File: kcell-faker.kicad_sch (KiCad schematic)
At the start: 19 parts, among them J4 DBG, SW1 BOOT, SW2 RST, SW3 UP, SW4 DOWN, U6 ESP32-S3-MINI-1

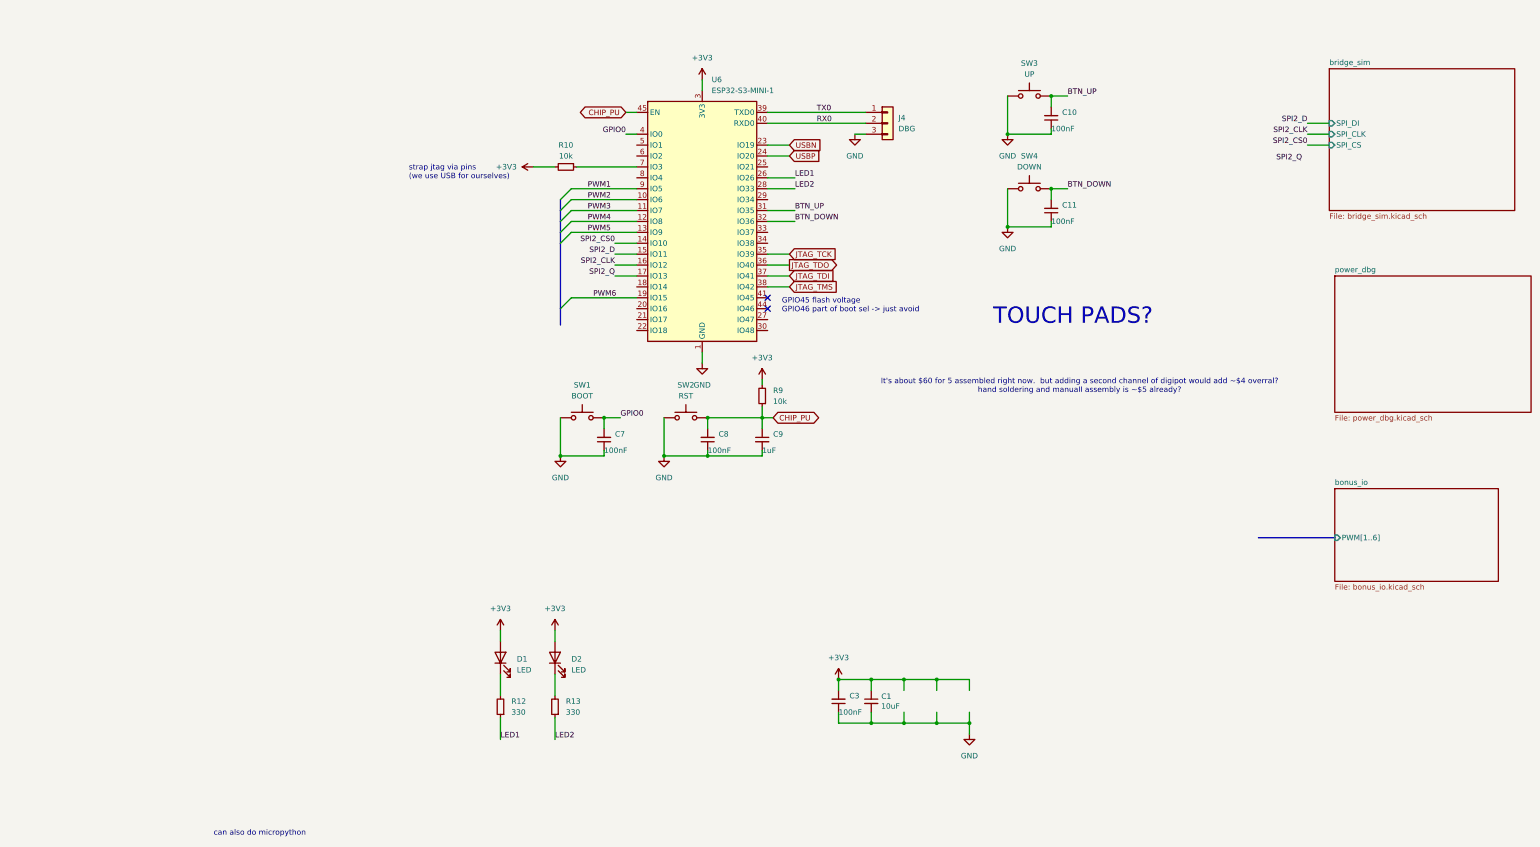
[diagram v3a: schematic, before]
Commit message: cleanup a bit
use red+green leds, sch on .100 grid, hook up more pins
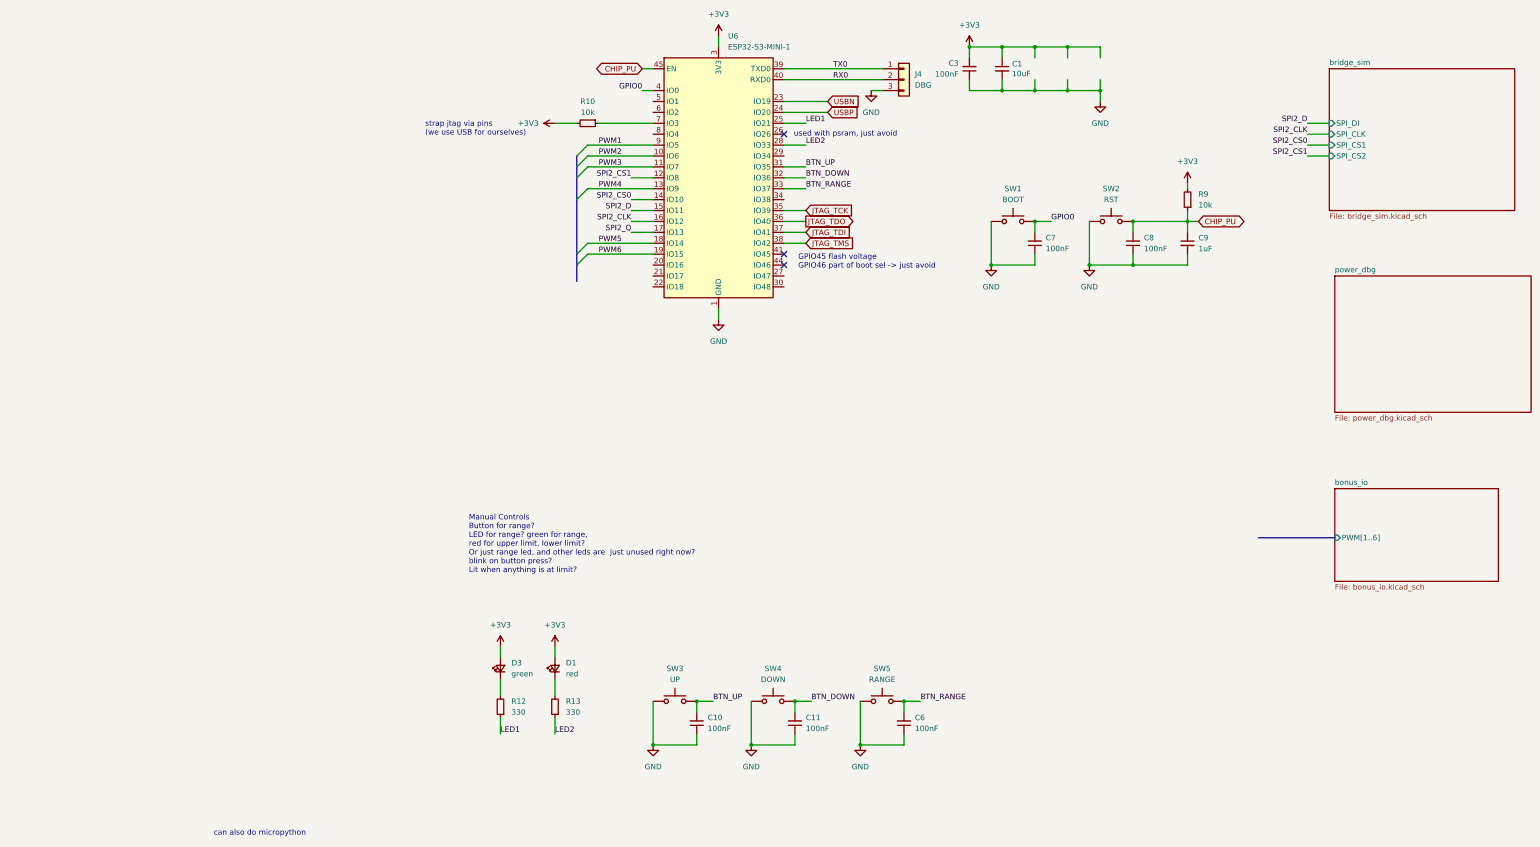
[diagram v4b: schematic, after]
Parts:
- removed D1, D2: LED, LED_SMD:LED_0603_1608Metric, symbol Device:LED
- added C6: 100nF, Capacitor_SMD:C_0603_1608Metric, symbol Device:C_Small
- added D1: red, LED_SMD:LED_0805_2012Metric, symbol Device:LED_Small
- added D3: green, LED_SMD:LED_0805_2012Metric, symbol Device:LED_Small
- added SW5: RANGE, Button_Switch_SMD:SW_SPST_TL3342, symbol Switch:SW_Push
- R10, R9: jlcbasic (none) -> basic
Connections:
- net +3V3: now also D1.2 (A), D3.2 (A)
- net GND: now also C6.1, SW5.1
- net LED1: now also U6.25 (IO21); no longer U6.26 (IO26)
- net PWM4: now also U6.13 (IO9); no longer U6.12 (IO8)
- net PWM5: now also U6.18 (IO14); no longer U6.13 (IO9)
- net BTN_RANGE: now reaches U6.33 (IO37)
- net BTN_RANGE: now also C6.2, SW5.2
- net at R13.2: now also D1.1 (K)
- net at R12.2: now also D3.1 (K)
- new net SPI2_CS1: U6.12 (IO8)
- no-connect marks 2 -> 3
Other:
- sheet bridge_sim ports: added SPI_CS1, SPI_CS2; removed SPI_CS
- note added: "Manual Controls Button for range? LED for range? green for range, red for upper limit, lower limit? Or just range led, and other leds are just unused right now? blink on button press? Lit when anything is at limit?"
- note added: "used with psram, just avoid"
- note removed: "It's about $60 for 5 assembled right now. but adding a second channel of digipot would add ~$4 overral? hand soldering and manuall assembly is ~$5 already?"
- note removed: "TOUCH PADS?"
- moved on the sheet: C1, C10, C11, C3, C7, C8, C9, J4, R10, R9, SW1, SW2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

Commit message: add the pwm method as an alternate impl
TODO: replace all resistors with 0805 so that precision _can_ be
soldered if desired
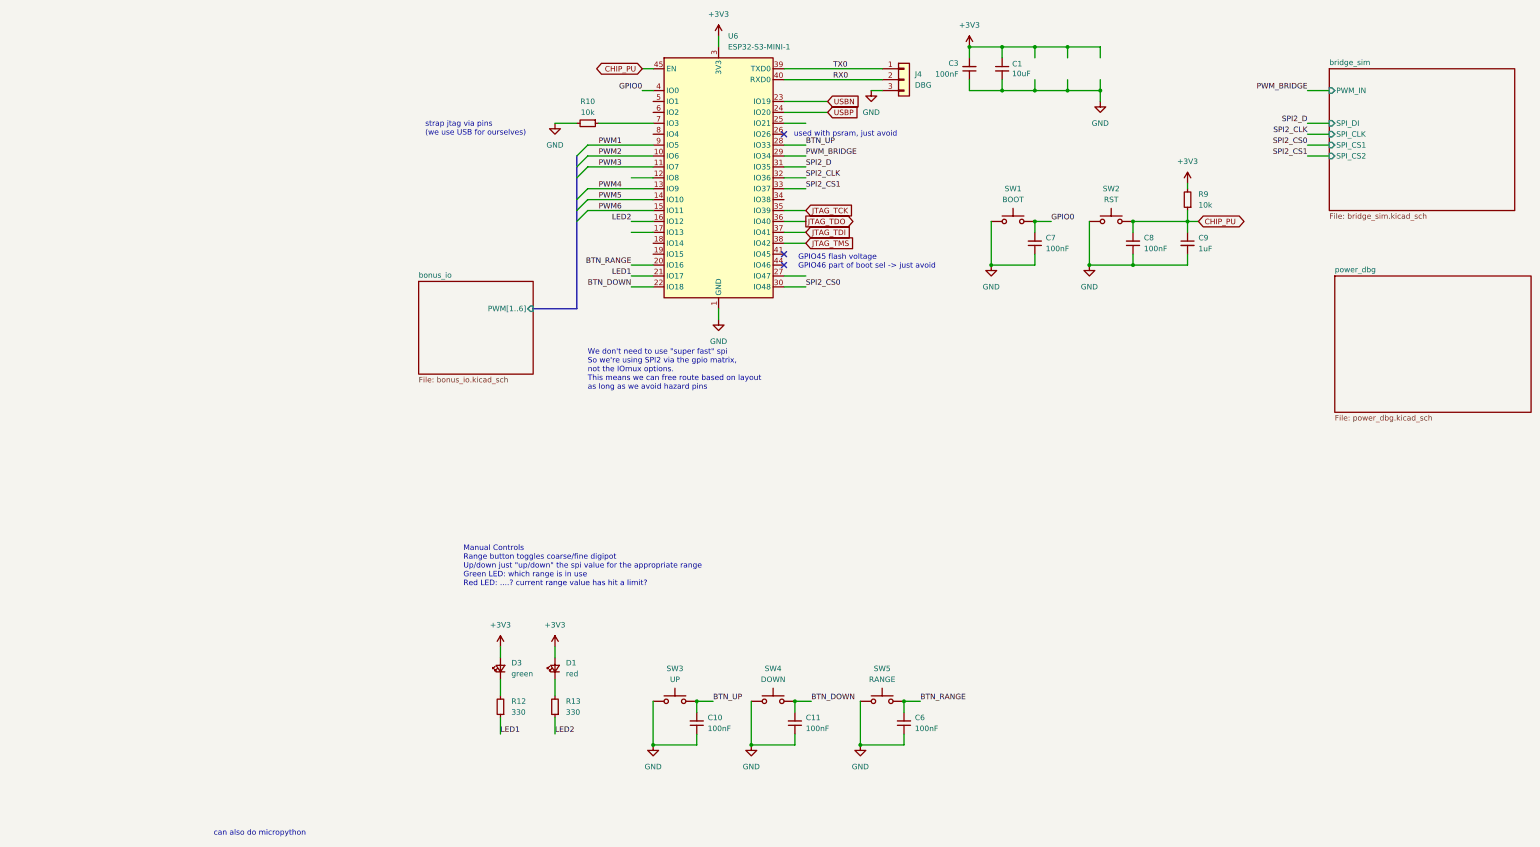
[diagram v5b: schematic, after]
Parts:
- SW1, SW2, SW3, SW4, SW5: jlcbasic (none) -> basic
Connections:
- net +3V3: no longer R10.2
- net BTN_DOWN: now also U6.22 (IO18); no longer U6.32 (IO36)
- net BTN_RANGE: now also U6.20 (IO16); no longer U6.33 (IO37)
- net BTN_UP: now also U6.28 (IO33); no longer U6.31 (IO35)
- net GND: now also R10.2
- net LED1: now also U6.21 (IO17); no longer U6.25 (IO21)
- net LED2: now also U6.16 (IO12); no longer U6.28 (IO33)
- net PWM5: now also U6.14 (IO10); no longer U6.18 (IO14)
- net PWM6: now also U6.15 (IO11); no longer U6.19 (IO15)
- net SPI2_CLK: now also U6.32 (IO36); no longer U6.16 (IO12)
- net SPI2_CS0: now also U6.30 (IO48); no longer U6.14 (IO10)
- net SPI2_CS1: now also U6.33 (IO37); no longer U6.12 (IO8)
- net SPI2_D: now also U6.31 (IO35); no longer U6.15 (IO11)
- net PWM_BRIDGE: now reaches U6.29 (IO34)
- net SPI2_Q: no longer names the net of U6.17 (IO13)
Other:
- sheet bridge_sim ports: added PWM_IN; removed none
- note added: "Manual Controls Range button toggles coarse/fine digipot Up/down just "up/down" the spi value for the appropriate range Green LED: which range is in use Red LED: ....? current range value has hit a limit?"
- note added: "We don't need to use "super fast" spi So we're using SPI2 via the gpio matrix, not the IOmux options. This means we can free route based on layout as long as we avoid hazard pins"
- note removed: "Manual Controls Button for range? LED for range? green for range, red for upper limit, lower limit? Or just range led, and other leds are just unused right now? blink on button press? Lit when anything is at limit?"
- title: (none) -> LoadCell Faker

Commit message: make a basic quick lib with jlc parts will  need extraction
Switch to 0805 for bridge resistors
switch to plain opto, we already have pulls and a fet.  (Could the other
one have directly pulled the resistor? (probably)
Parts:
- C1: LCSC Part# (none) -> C15850; lcsc# C15850 -> (none)
- C10, C11, C3, C6, C7, C8: LCSC Part# (none) -> C14663; lcsc# C14663 -> (none)
- C9: LCSC Part# (none) -> C15849; lcsc# C15849 -> (none)
- D1: LCSC Part# (none) -> C84256; lcsc# C84256 -> (none)
- D3: LCSC Part# (none) -> C2297; lcsc# C2297 -> (none)
- J4: LCSC Part# (none) -> C2937625; lcsc# C2937625 -> (none)
- R10, R9: LCSC Part# (none) -> C25804; lcsc# C25804 -> (none)
- R12, R13: LCSC Part# (none) -> C23138; lcsc# C23138 -> (none)
- SW1, SW2, SW3, SW4, SW5: LCSC Part# (none) -> C318884; lcsc# C318884 -> (none)
- U6: LCSC Part# (none) -> C2913206; lcsc# C2913206 -> (none)
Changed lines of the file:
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@@
 			)
 		)
-		(property "lcsc#" "C14663"
+		(property "jlc-basic" "1"
 			(at 104.14 182.88 0)
 			(effects
@@
 			)
 		)
-		(property "jlc-basic" "1"
+		(property "lcsc2#" ""
 			(at 104.14 182.88 0)
 			(effects
@@
 			)
 		)
-		(property "lcsc2#" ""
+		(property "jlcbasic" "basic"
 			(at 104.14 182.88 0)
 			(effects
@@
 			)
 		)
-		(property "jlcbasic" "basic"
+		(property "LCSC Part#" "C14663"
 			(at 104.14 182.88 0)
 			(effects
@@
 			)
 		)
-		(property "lcsc#" "C2913206"
+		(property "LCSC Part#" "C2913206"
 			(at 86.36 55.88 0)
 			(effects
@@
 			)
 		)
-		(property "lcsc#" "C318884"
+		(property "MPN" "TS-1187A-B-A-B"
 			(at 99.06 177.8 0)
 			(effects
@@
 			)
 		)
-		(property "MPN" "TS-1187A-B-A-B"
+		(property "jlc-basic" "1"
 			(at 99.06 177.8 0)
 			(effects
@@
 			)
 		)
-		(property "jlc-basic" "1"
+		(property "lcsc2#" ""
 			(at 99.06 177.8 0)
 			(effects
@@
 			)
 		)
-		(property "lcsc2#" ""
+		(property "jlcbasic" "basic"
 			(at 99.06 177.8 0)
 			(effects
@@
 			)
 		)
-		(property "jlcbasic" "basic"
+		(property "LCSC Part#" "C318884"
 			(at 99.06 177.8 0)
 			(effects
@@
 			)
 		)
-		(property "lcsc#" "C14663"
+		(property "jlc-basic" "1"
 			(at 81.28 182.88 0)
 			(effects
@@
 			)
 		)
-		(property "jlc-basic" "1"
+		(property "lcsc2#" ""
 			(at 81.28 182.88 0)
 			(effects
@@
 			)
 		)
-		(property "lcsc2#" ""
+		(property "jlcbasic" "basic"
 			(at 81.28 182.88 0)
 			(effects
@@
 			)
 		)
-		(property "jlcbasic" "basic"
+		(property "LCSC Part#" "C14663"
 			(at 81.28 182.88 0)
 			(effects
@@
 			)
 		)
-		(property "lcsc#" "C318884"
+		(property "MPN" "TS-1187A-B-A-B"
 			(at 177.8 66.04 0)
 			(effects
@@
 			)
 		)
-		(property "MPN" "TS-1187A-B-A-B"
+		(property "jlc-basic" "1"
 			(at 177.8 66.04 0)
 			(effects
@@
 			)
 		)
-		(property "jlc-basic" "1"
+		(property "lcsc2#" ""
 			(at 177.8 66.04 0)
 			(effects
@@
 			)
 		)
-		(property "lcsc2#" ""
+		(property "jlcbasic" "basic"
 			(at 177.8 66.04 0)
 			(effects
@@
 			)
 		)
-		(property "jlcbasic" "basic"
+		(property "LCSC Part#" "C318884"
 			(at 177.8 66.04 0)
 			(effects
@@
 			)
 		)
-		(property "lcsc#" "C2297"
+		(property "LCSC Part#" "C2297"
 			(at 35.56 170.18 0)
 			(effects
@@
 			)
 		)
-		(property "lcsc#" "C23138"
+		(property "jlcbasic" "basic"
 			(at 48.26 179.07 0)
 			(effects
@@
 			)
 		)
-		(property "jlcbasic" "basic"
+		(property "LCSC Part#" "C23138"
 			(at 48.26 179.07 0)
 			(effects
@@
 			)
 		)
-		(property "lcsc#" "C14663"
+		(property "jlc-basic" "1"
 			(at 129.54 182.88 0)
 			(effects
@@
 			)
 		)
-		(property "jlc-basic" "1"
+		(property "lcsc2#" ""
 			(at 129.54 182.88 0)
 			(effects
@@
 			)
 		)
-		(property "lcsc2#" ""
+		(property "jlcbasic" "basic"
 			(at 129.54 182.88 0)
 			(effects
@@
 			)
 		)
-		(property "jlcbasic" "basic"
+		(property "LCSC Part#" "C14663"
 			(at 129.54 182.88 0)
 			(effects
@@
 			)
 		)
-		(property "lcsc#" "C25804"
+		(property "lcsc2#" ""
 			(at 195.58 60.96 0)
 			(effects
@@
 			)
 		)
-		(property "lcsc2#" ""
+		(property "jlcbasic" "basic"
 			(at 195.58 60.96 0)
 			(effects
@@
 			)
 		)
-		(property "jlcbasic" "basic"
+		(property "LCSC Part#" "C25804"
 			(at 195.58 60.96 0)
 			(effects
@@
 			)
 		)
-		(property "lcsc#" "C14663"
+		(property "jlc-basic" "1"
 			(at 182.88 71.12 0)
 			(effects
@@
 			)
 		)
-		(property "jlc-basic" "1"
+		(property "lcsc2#" ""
 			(at 182.88 71.12 0)
 			(effects
@@
 			)
 		)
-		(property "lcsc2#" ""
+		(property "jlcbasic" "basic"
 			(at 182.88 71.12 0)
 			(effects
@@
 			)
 		)
-		(property "jlcbasic" "basic"
+		(property "LCSC Part#" "C14663"
 			(at 182.88 71.12 0)
 			(effects
@@
 			)
 		)
-		(property "lcsc#" "C15849"
+		(property "lcsc2#" ""
 			(at 195.58 71.12 0)
 			(effects
@@
 			)
 		)
-		(property "lcsc2#" ""
+		(property "jlcbasic" "basic"
 			(at 195.58 71.12 0)
 			(effects
@@
 			)
 		)
-		(property "jlcbasic" "basic"
+		(property "LCSC Part#" "C15849"
 			(at 195.58 71.12 0)
 			(effects
@@
 			)
 		)
-		(property "lcsc#" "C25804"
+		(property "lcsc2#" ""
 			(at 55.88 43.18 0)
 			(effects
@@
 			)
 		)
-		(property "lcsc2#" ""
+		(property "jlcbasic" "basic"
 			(at 55.88 43.18 0)
 			(effects
@@
 			)
 		)
-		(property "jlcbasic" "basic"
+		(property "LCSC Part#" "C25804"
 			(at 55.88 43.18 0)
 			(effects
@@
 			)
 		)
-		(property "lcsc#" "C15850"
+		(property "jlc-basic" "1"
 			(at 152.4 30.48 0)
 			(effects
@@
 			)
 		)
-		(property "jlc-basic" "1"
+		(property "LCSC Part#" "C15850"
 			(at 152.4 30.48 0)
 			(effects
@@
 			)
 		)
-		(property "lcsc#" "C318884"
+		(property "MPN" "TS-1187A-B-A-B"
 			(at 76.2 177.8 0)
 			(effects
@@
 			)
 		)
-		(property "MPN" "TS-1187A-B-A-B"
+		(property "jlc-basic" "1"
 			(at 76.2 177.8 0)
 			(effects
@@
 			)
 		)
-		(property "jlc-basic" "1"
+		(property "lcsc2#" ""
 			(at 76.2 177.8 0)
 			(effects
@@
 			)
 		)
-		(property "lcsc2#" ""
+		(property "jlcbasic" "basic"
 			(at 76.2 177.8 0)
 			(effects
@@
 			)
 		)
-		(property "jlcbasic" "basic"
+		(property "LCSC Part#" "C318884"
 			(at 76.2 177.8 0)
 			(effects
@@
 			)
 		)
-		(property "lcsc#" "C84256"
+		(property "LCSC Part#" "C84256"
 			(at 48.26 170.18 0)
 			(effects
@@
 			)
 		)
-		(property "lcsc#" "C23138"
+		(property "jlcbasic" "basic"
 			(at 35.56 179.07 0)
 			(effects
@@
 			)
 		)
-		(property "jlcbasic" "basic"
+		(property "LCSC Part#" "C23138"
 			(at 35.56 179.07 0)
 			(effects
@@
 			)
 		)
-		(property "lcsc#" "C2937625"
+		(property "LCSC Part#" "C2937625"
 			(at 129.54 33.02 0)
 			(effects
@@
 			)
 		)
-		(property "lcsc#" "C14663"
+		(property "jlc-basic" "1"
 			(at 160.02 71.12 0)
 			(effects
@@
 			)
 		)
-		(property "jlc-basic" "1"
+		(property "lcsc2#" ""
 			(at 160.02 71.12 0)
 			(effects
@@
 			)
 		)
-		(property "lcsc2#" ""
+		(property "jlcbasic" "basic"
 			(at 160.02 71.12 0)
 			(effects
@@
 			)
 		)
-		(property "jlcbasic" "basic"
+		(property "LCSC Part#" "C14663"
 			(at 160.02 71.12 0)
 			(effects
@@
 			)
 		)
-		(property "lcsc#" "C318884"
+		(property "MPN" "TS-1187A-B-A-B"
 			(at 154.94 66.04 0)
 			(effects
@@
 			)
 		)
-		(property "MPN" "TS-1187A-B-A-B"
+		(property "jlc-basic" "1"
 			(at 154.94 66.04 0)
 			(effects
@@
 			)
 		)
-		(property "jlc-basic" "1"
+		(property "lcsc2#" ""
 			(at 154.94 66.04 0)
 			(effects
@@
 			)
 		)
-		(property "lcsc2#" ""
+		(property "jlcbasic" "basic"
 			(at 154.94 66.04 0)
 			(effects
@@
 			)
 		)
-		(property "jlcbasic" "basic"
+		(property "LCSC Part#" "C318884"
 			(at 154.94 66.04 0)
 			(effects
@@
 			)
 		)
-		(property "lcsc#" "C318884"
+		(property "MPN" "TS-1187A-B-A-B"
 			(at 124.46 177.8 0)
 			(effects
@@
 			)
 		)
-		(property "MPN" "TS-1187A-B-A-B"
+		(property "jlc-basic" "1"
 			(at 124.46 177.8 0)
 			(effects
@@
 			)
 		)
-		(property "jlc-basic" "1"
+		(property "lcsc2#" ""
 			(at 124.46 177.8 0)
 			(effects
@@
 			)
 		)
-		(property "lcsc2#" ""
+		(property "jlcbasic" "basic"
 			(at 124.46 177.8 0)
 			(effects
@@
 			)
 		)
-		(property "jlcbasic" "basic"
+		(property "LCSC Part#" "C318884"
 			(at 124.46 177.8 0)
 			(effects
@@
 			)
 		)
-		(property "lcsc#" "C14663"
+		(property "jlc-basic" "1"
 			(at 144.78 30.48 0)
 			(effects
@@
 			)
 		)
-		(property "jlc-basic" "1"
+		(property "lcsc2#" ""
 			(at 144.78 30.48 0)
 			(effects
@@
 			)
 		)
-		(property "lcsc2#" ""
+		(property "jlcbasic" "basic"
 			(at 144.78 30.48 0)
 			(effects
@@
 			)
 		)
-		(property "jlcbasic" "basic"
+		(property "LCSC Part#" "C14663"
 			(at 144.78 30.48 0)
 			(effects
